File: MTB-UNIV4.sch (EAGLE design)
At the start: 119 parts, among them IC1 MEGA128-A, IC2 SN75176BP, IC3 MC7805CDTG, IC4 ULN2803A, IC5 ULN2803A, Q1 14.745 MHz, X1A MVE252-5-V, X1B MVE252-5-V, X2A MVE252-5-V, X2B MVE252-5-V, X3 1751316, X4 1751316, X5 1751316, X6 1751316

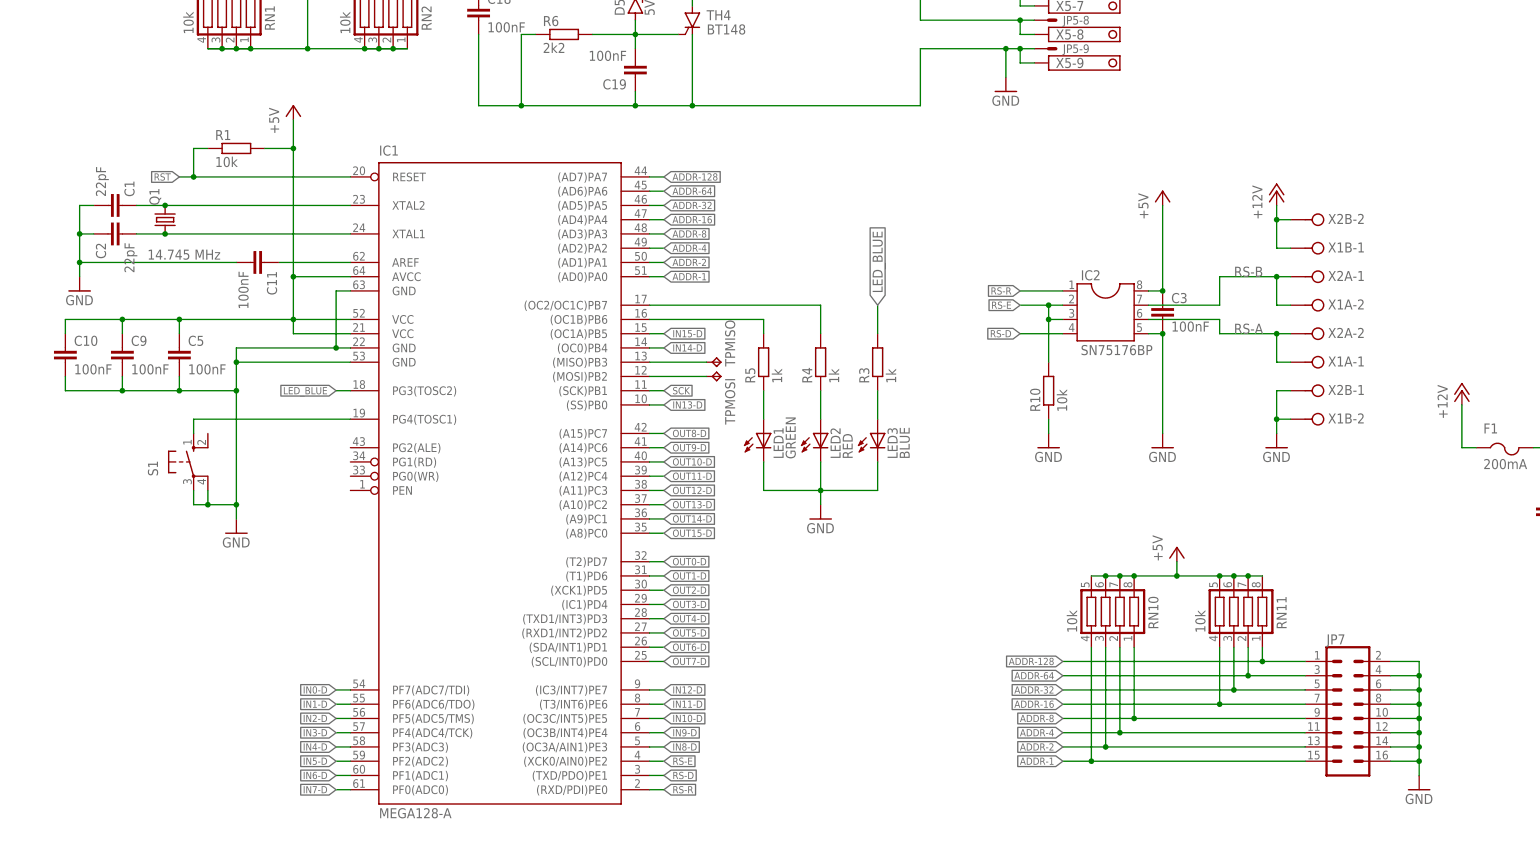
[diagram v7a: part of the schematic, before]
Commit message: Use 75176 part from standard library.
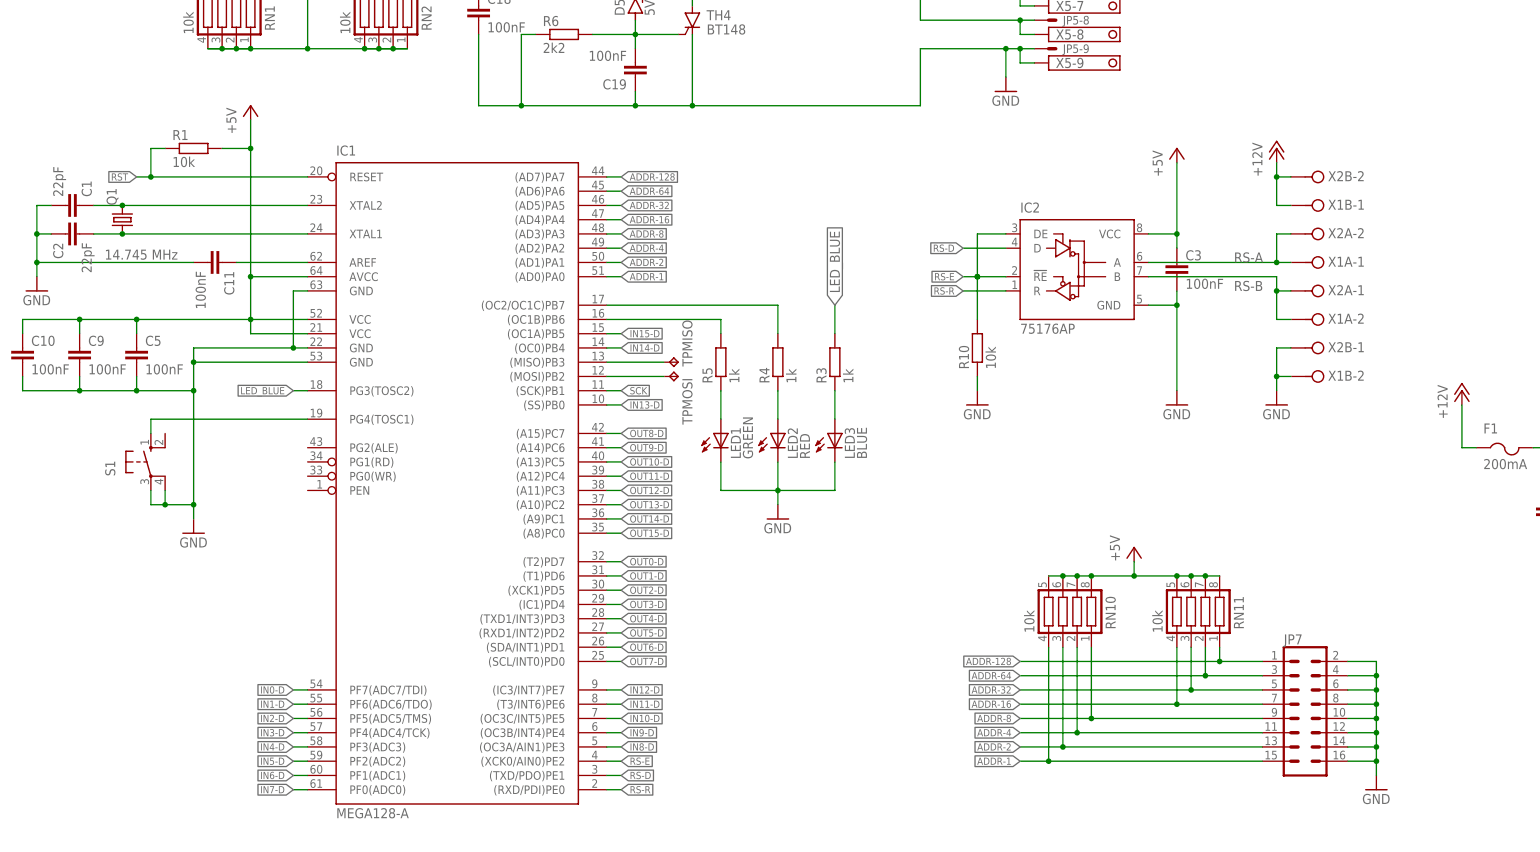
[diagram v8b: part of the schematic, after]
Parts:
- IC2: value SN75176BP -> 75176AP; device ic-package:DIL8 -> 751xx:75176AP
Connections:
- net +5V: now also IC2.VCC; no longer IC2.8
- net GND: now also IC2.GND; no longer IC2.5
- net RS-A: now also IC2.A; no longer IC2.6
- net RS-B: now also IC2.B; no longer IC2.7
- net RS-D: now also IC2.D; no longer IC2.4
- net RS-E: now also IC2.!RE, IC2.DE; no longer IC2.2, IC2.3
- net RS-R: now also IC2.R; no longer IC2.1
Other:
- moved on the sheet: C1, C10, C11, C2, C3, C5, C9, IC1, JP7, LED1, LED2, LED3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
